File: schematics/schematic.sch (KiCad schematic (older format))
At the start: 5 parts, among them J1 Left rail FirebeetleESP8266, J2 Right rail FirebeetleESP8266, SW1 NO

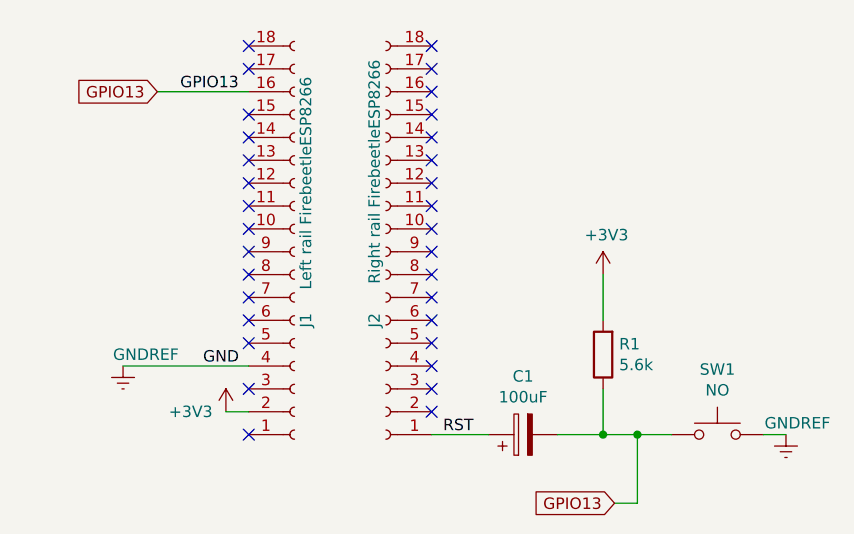
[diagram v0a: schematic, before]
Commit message: Add BME680 to schematic
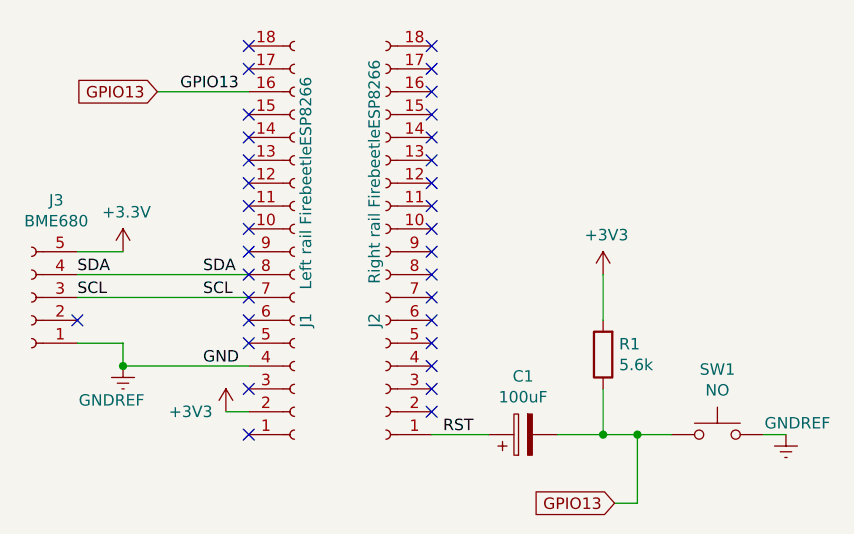
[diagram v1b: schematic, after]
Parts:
- added J3: BME680, symbol Connector:Conn_01x05_Female
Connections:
- net +3V3: now also J3.5 (Pin_5)
- net GNDREF: now also J3.1 (Pin_1)
- net SCL: now reaches J1.7 (Pin_7)
- net SCL: now also J3.3 (Pin_3)
- net SDA: now reaches J1.8 (Pin_8)
- net SDA: now also J3.4 (Pin_4)
- no-connect marks 32 -> 33
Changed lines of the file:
@@
 Text Label 2500 1950 0    50   ~ 0
 GPIO13
-Text Label 2600 3150 0    50   ~ 0
-GND
 $Comp
 L Switch:SW_Push SW1
@@
 $EndComp
 $Comp
-L power:GNDREF #PWR0102
-U 1 1 5F4E7867
-P 2250 3150
-F 0 "#PWR0102" H 2250 2900 50  0001 C CNN
-F 1 "GNDREF" H 2350 3200 50  0000 C CNN
-F 2 "" H 2250 3150 50  0001 C CNN
-F 3 "" H 2250 3150 50  0001 C CNN
-	1    2250 3150
-	1    0    0    -1
-$EndComp
-Wire Wire Line
-	2250 3150 2800 3150
-$Comp
 L power:+3V3 #PWR0103
 U 1 1 5F4E90EE
@@
 $EndComp
 NoConn ~ 2800 3450
+NoConn ~ 2050 2950
+Wire Wire Line
+	2050 2650 2250 2650
+$Comp
+L power:+3.3V #PWR?
+U 1 1 5F56A445
+P 2250 2650
+F 0 "#PWR?" H 2250 2500 50  0001 C CNN
+F 1 "+3.3V" H 2265 2823 50  0000 C CNN
+F 2 "" H 2250 2650 50  0001 C CNN
+F 3 "" H 2250 2650 50  0001 C CNN
+	1    2250 2650
+	1    0    0    -1
+$EndComp
+$Comp
+L Connector:Conn_01x05_Female J3
+U 1 1 5F567389
+P 1850 2850
+F 0 "J3" H 1742 2425 50  0000 C CNN
+F 1 "BME680" H 1742 2516 50  0000 C CNN
+F 2 "" H 1850 2850 50  0001 C CNN
+F 3 "~" H 1850 2850 50  0001 C CNN
+	1    1850 2850
+	-1   0    0    1
+$EndComp
+Wire Wire Line
+	2250 3150 2800 3150
+$Comp
+L power:GNDREF #PWR0102
+U 1 1 5F4E7867
+P 2250 3150
+F 0 "#PWR0102" H 2250 2900 50  0001 C CNN
+F 1 "GNDREF" H 2200 3000 50  0000 C CNN
+F 2 "" H 2250 3150 50  0001 C CNN
+F 3 "" H 2250 3150 50  0001 C CNN
+	1    2250 3150
+	1    0    0    -1
+$EndComp
+Text Label 2600 3150 0    50   ~ 0
+GND
+Wire Wire Line
+	2050 2750 2800 2750
+Wire Wire Line
+	2050 2850 2800 2850
+Wire Wire Line
+	2050 3050 2250 3050
+Wire Wire Line
+	2250 3050 2250 3150
+Connection ~ 2250 3150
+Text Label 2600 2750 0    50   ~ 0
+SDA
+Text Label 2600 2850 0    50   ~ 0
+SCL
+Text Label 2050 2750 0    50   ~ 0
+SDA
+Text Label 2050 2850 0    50   ~ 0
+SCL
 $EndSCHEMATC
